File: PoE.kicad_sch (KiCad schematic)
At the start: 73 parts, among them Q2 FDMS86255, U20 TPS23734, U23 TCMT1107

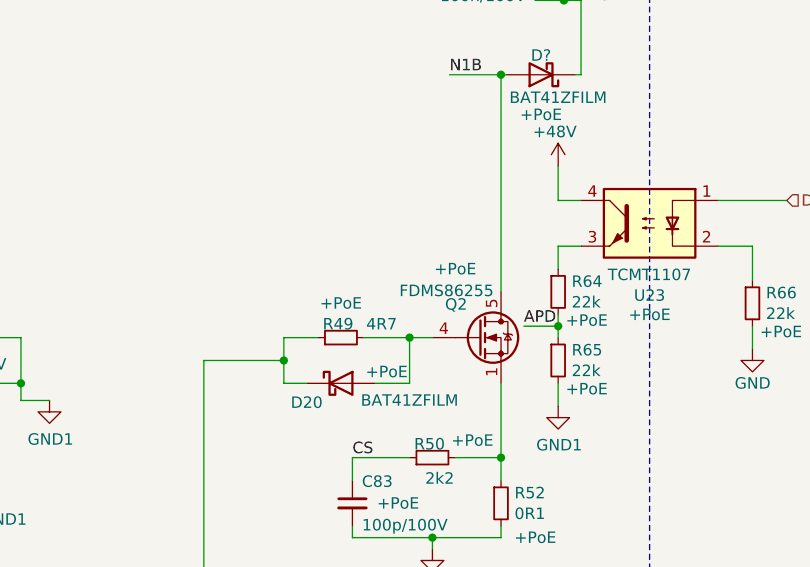
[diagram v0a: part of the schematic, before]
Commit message: Adjust Manufacturer/PartNumber for some parts
- Use Diodes B2100-13-F consistently
- Define part for pin headers
- Replace N-Channel MOSFET for PoE with BSZ440N10NS3GATMA1
- Define Input protection MOSFET DMP3013SFV-7

Signed-off-by: Stefan Agner <stefan@agner.ch>
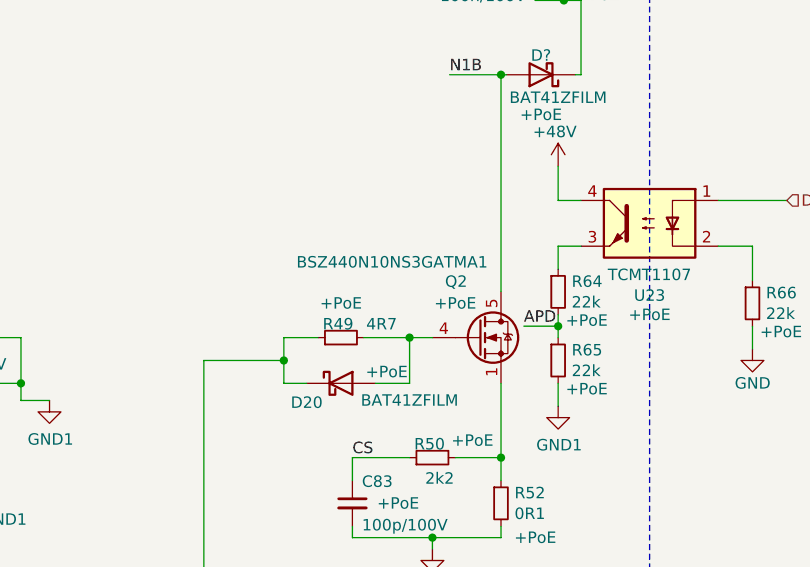
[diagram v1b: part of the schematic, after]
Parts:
- D18: PartNumber B3100-13-F -> B2100-13-F
- Q2: value FDMS86255 -> BSZ440N10NS3GATMA1; symbol Transistor_FET:FDMS86255 -> Transistor_FET:BSC440N10NS3G; Manufacturer ON Semiconductor -> Infineon Technologies; PartNumber FDMS86255 -> BSZ440N10NS3GATMA1
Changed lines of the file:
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@@
   (symbol (lib_id "power:GND1") (at 67.945 174.625 0) (unit 1)
     (in_bom yes) (on_board yes)
-    (property "Reference" "#PWR?" (id 0) (at 67.945 180.975 0)
+    (property "Reference" "#PWR0267" (id 0) (at 67.945 180.975 0)
       (effects (font (size 1.27 1.27)) hide)
     )
@@
   (symbol (lib_id "power:GND1") (at 121.92 129.54 90) (unit 1)
     (in_bom yes) (on_board yes)
-    (property "Reference" "#PWR?" (id 0) (at 128.27 129.54 0)
+    (property "Reference" "#PWR0270" (id 0) (at 128.27 129.54 0)
       (effects (font (size 1.27 1.27)) hide)
     )
@@
   (symbol (lib_id "power:GND1") (at 158.75 189.865 0) (unit 1)
     (in_bom yes) (on_board yes)
-    (property "Reference" "#PWR?" (id 0) (at 158.75 196.215 0)
+    (property "Reference" "#PWR0264" (id 0) (at 158.75 196.215 0)
       (effects (font (size 1.27 1.27)) hide)
     )
@@
   (symbol (lib_id "power:GND1") (at 165.1 64.77 0) (unit 1)
     (in_bom yes) (on_board yes)
-    (property "Reference" "#PWR?" (id 0) (at 165.1 71.12 0)
+    (property "Reference" "#PWR0269" (id 0) (at 165.1 71.12 0)
       (effects (font (size 1.27 1.27)) hide)
     )
@@
   (symbol (lib_id "power:GND1") (at 189.23 24.13 0) (unit 1)
     (in_bom yes) (on_board yes)
-    (property "Reference" "#PWR?" (id 0) (at 189.23 30.48 0)
+    (property "Reference" "#PWR0268" (id 0) (at 189.23 30.48 0)
       (effects (font (size 1.27 1.27)) hide)
     )
@@
   (symbol (lib_id "power:GND") (at 205.74 25.4 0) (unit 1)
     (in_bom yes) (on_board yes)
-    (property "Reference" "#PWR?" (id 0) (at 205.74 31.75 0)
+    (property "Reference" "#PWR0272" (id 0) (at 205.74 31.75 0)
       (effects (font (size 1.27 1.27)) hide)
     )
@@
   (symbol (lib_id "power:GND") (at 212.09 53.975 0) (unit 1)
     (in_bom yes) (on_board yes)
-    (property "Reference" "#PWR?" (id 0) (at 212.09 60.325 0)
+    (property "Reference" "#PWR0271" (id 0) (at 212.09 60.325 0)
       (effects (font (size 1.27 1.27)) hide)
     )
@@
   (symbol (lib_id "power:GND") (at 240.03 45.72 0) (unit 1)
     (in_bom yes) (on_board yes)
-    (property "Reference" "#PWR?" (id 0) (at 240.03 52.07 0)
+    (property "Reference" "#PWR0274" (id 0) (at 240.03 52.07 0)
       (effects (font (size 1.27 1.27)) hide)
     )
@@
   (symbol (lib_id "power:GND") (at 247.015 45.72 0) (unit 1)
     (in_bom yes) (on_board yes)
-    (property "Reference" "#PWR?" (id 0) (at 247.015 52.07 0)
+    (property "Reference" "#PWR0275" (id 0) (at 247.015 52.07 0)
       (effects (font (size 1.27 1.27)) hide)
     )
@@
   (symbol (lib_id "power:GND") (at 273.05 45.72 0) (unit 1)
     (in_bom yes) (on_board yes)
-    (property "Reference" "#PWR?" (id 0) (at 273.05 52.07 0)
+    (property "Reference" "#PWR0273" (id 0) (at 273.05 52.07 0)
       (effects (font (size 1.27 1.27)) hide)
     )
@@
       (effects (font (size 1.27 1.27)) hide)
     )
-    (property "PartNumber" "B3100-13-F" (id 6) (at 92.71 173.99 0)
+    (property "PartNumber" "B2100-13-F" (id 6) (at 92.71 173.99 0)
       (effects (font (size 1.27 1.27)) hide)
     )
@@
     (pin "2")
   )
-  (symbol (lib_id "Transistor_FET:FDMS86255") (at 180.34 109.22 0) (unit 1)
-    (in_bom yes) (on_board yes)
-    (property "Reference" "Q2" (id 0) (at 176.6571 105.5306 0)
-      (effects (font (size 1.27 1.27)) (justify left))
-    )
-    (property "Value" "FDMS86255" (id 1) (at 171.5771 104.0193 0)
+  (symbol (lib_id "Transistor_FET:BSC440N10NS3G") (at 180.34 109.22 0) (unit 1)
+    (in_bom yes) (on_board yes)
+    (property "Reference" "Q2" (id 0) (at 176.6571 102.9906 0)
+      (effects (font (size 1.27 1.27)) (justify left))
+    )
+    (property "Value" "BSZ440N10NS3GATMA1" (id 1) (at 160.1471 100.8443 0)
       (effects (font (size 1.27 1.27)) (justify left))
     )
@@
       (effects (font (size 1.27 1.27) italic) (justify left) hide)
     )
-    (property "Datasheet" "https://www.onsemi.com/pub/Collateral/FDMS86255-D.pdf" (id 3) (at 180.34 109.22 90)
+    (property "Datasheet" "http://www.infineon.com/dgdl/Infineon-BSC440N10NS3-DS-v02_04-en.pdf?fileId=db3a30432239cccd0122604520d47f56" (id 3) (at 180.34 109.22 90)
       (effects (font (size 1.27 1.27)) (justify left) hide)
     )
-    (property "Config" "+PoE" (id 4) (at 177.8 101.6 0))
-    (property "Manufacturer" "ON Semiconductor" (id 5) (at 180.34 109.22 0)
-      (effects (font (size 1.27 1.27)) hide)
-    )
-    (property "PartNumber" "FDMS86255" (id 6) (at 180.34 109.22 0)
-      (effects (font (size 1.27 1.27)) hide)
-    )
+    (property "Config" "+PoE" (id 4) (at 177.8 105.41 0))
+    (property "Manufacturer" "Infineon Technologies" (id 5) (at 180.34 109.22 0)
+      (effects (font (size 1.27 1.27)) hide)
+    )
+    (property "PartNumber" "BSZ440N10NS3GATMA1" (id 6) (at 180.34 109.22 0)
+      (effects (font (size 1.27 1.27)) hide)
+    )

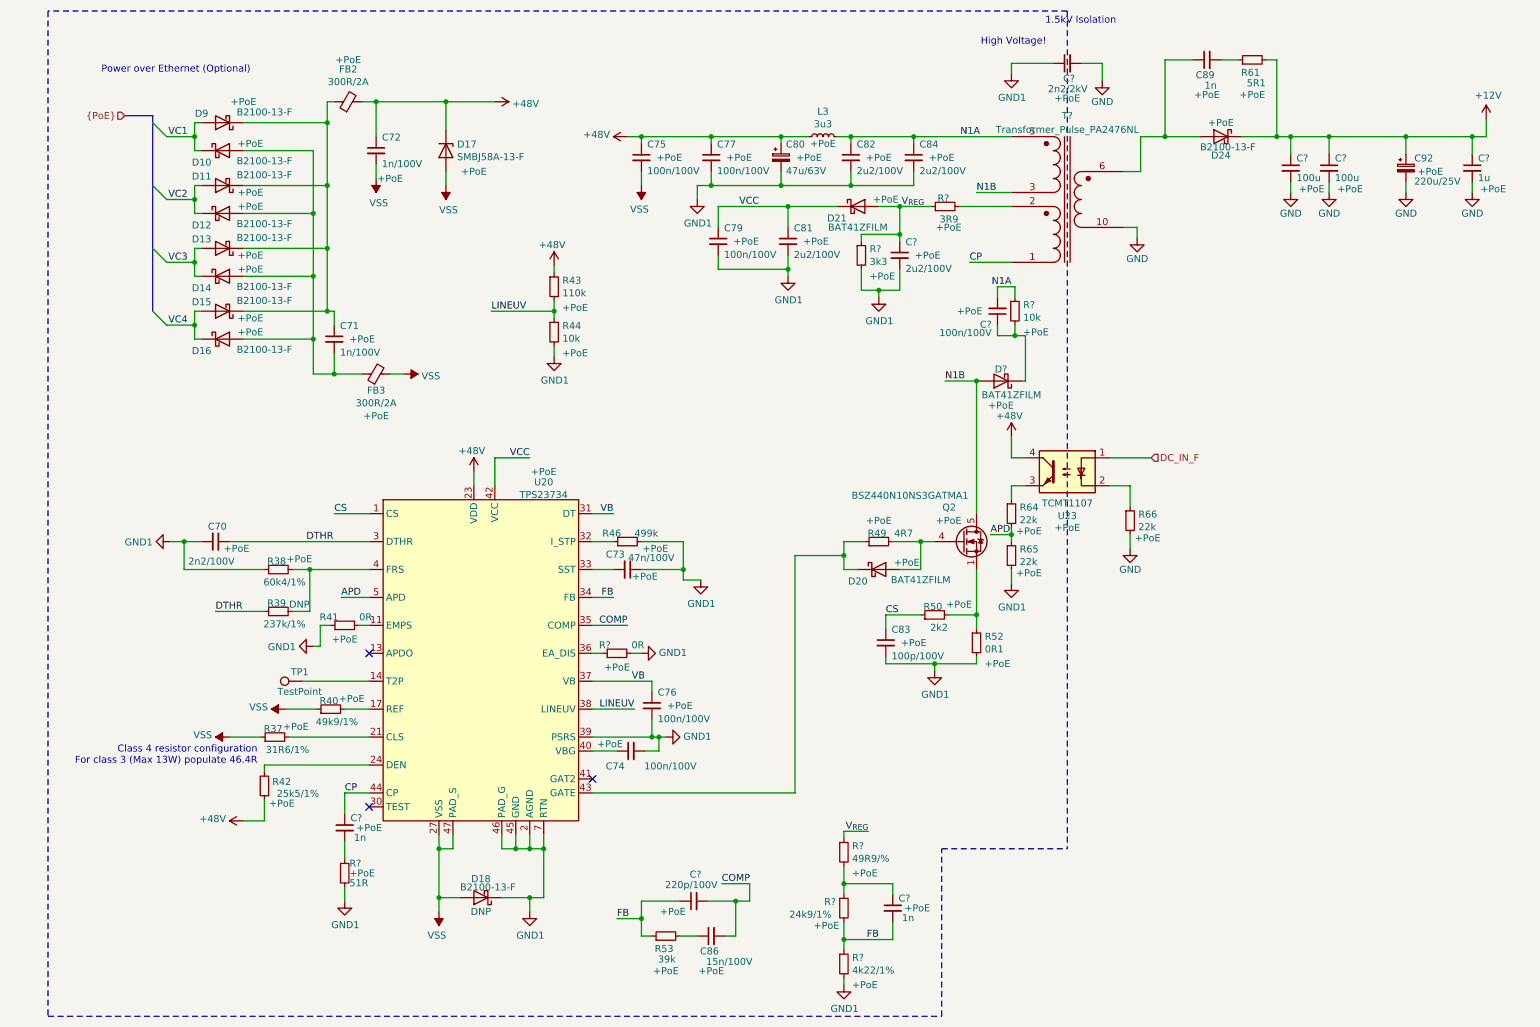
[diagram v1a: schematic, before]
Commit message: Adjust various parts to improve BOM
- Replace unusual/high value ceramics with lower value in parallel
- Use the same protection Shottky Diode in PoE as in regular input
  (B340LB-13-F)
- Replace PoE rectifier Diodes with B1100-13-F
- Replace PoE Inductor (SRN6045TA-3R3Y) with the same part from 5V power
  supply (Taiyo Yuden NRS8030T3R3MJGJ)
- Correctly specify Pulse Electronics transformer

Signed-off-by: Stefan Agner <stefan@agner.ch>
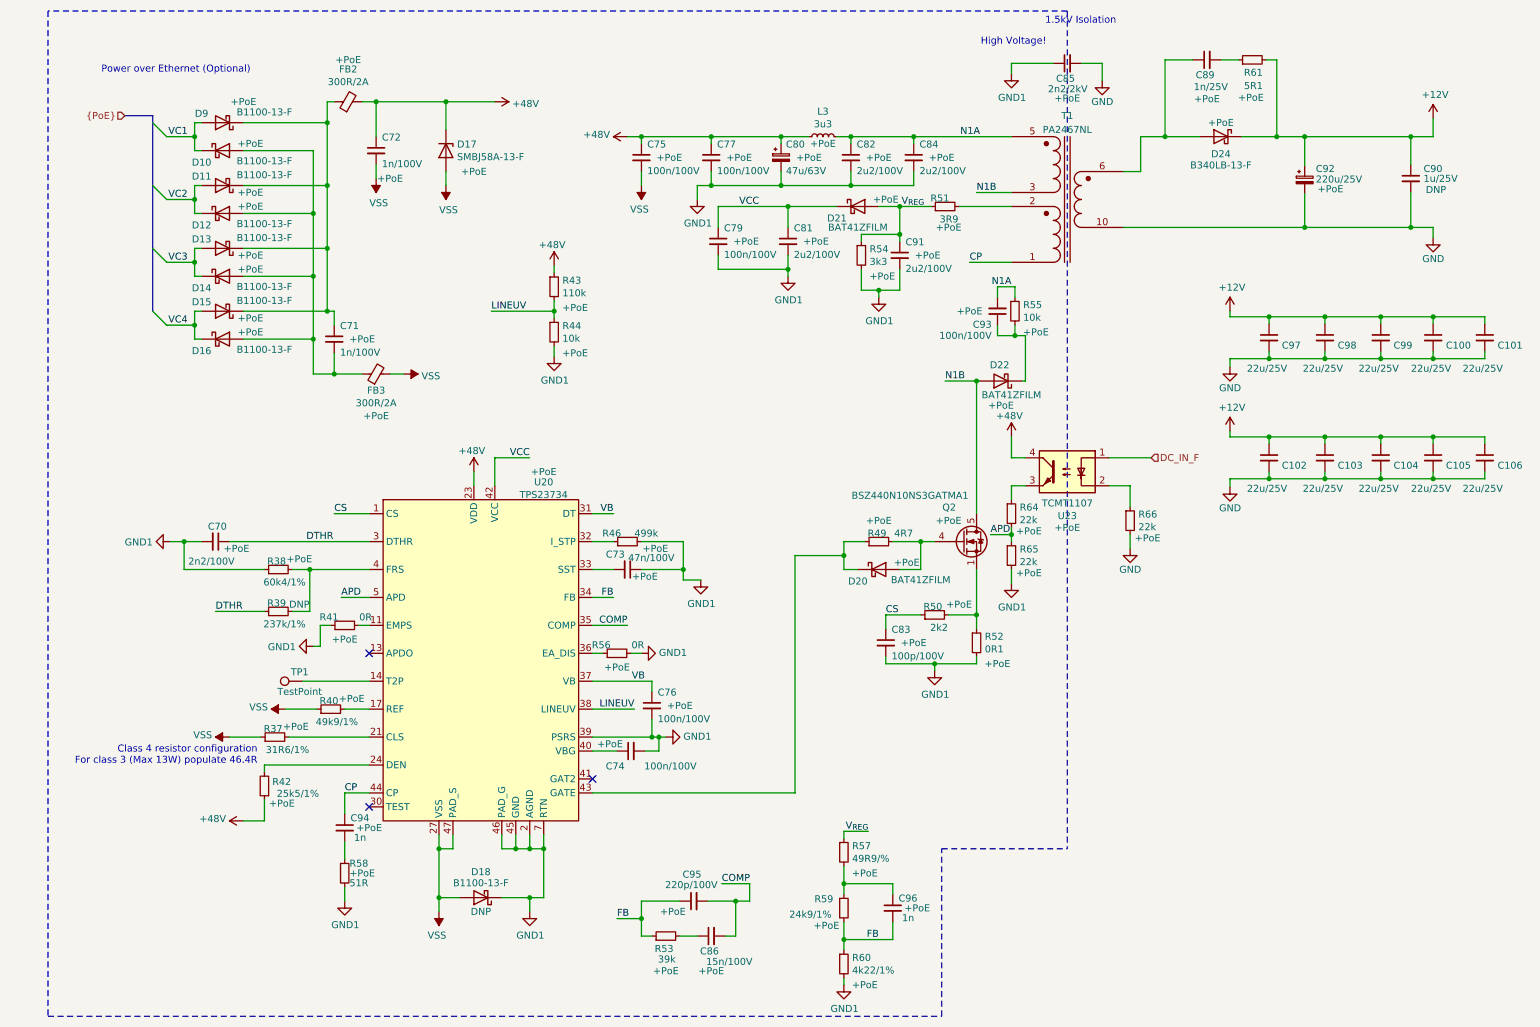
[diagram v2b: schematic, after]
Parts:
- removed C? (x2): 100u, Capacitor_SMD:C_0402_1005Metric, symbol Device:C_Small
- added C100, C101, C102, C103, C104, C105, C106, C97, C98, C99: 22u/25V, Capacitor_SMD:C_0805_2012Metric, symbol Device:C_Small
- C89: value 1n -> 1n/25V
- C90: renamed from C?; value 1u -> 1u/25V; Config +PoE -> DNP
- D10, D11, D12, D13, D14, D15, D16, D18, D9: value B2100-13-F -> B1100-13-F; footprint Diode_SMD:D_SMB -> Diode_SMD:D_SMA; PartNumber B2100-13-F -> B1100-13-F
- D24: value B2100-13-F -> B340LB-13-F; PartNumber B3100-13-F -> B340LB-13-F
- L3: footprint Inductor_SMD:L_Bourns_SRN6045TA -> Inductor_SMD:L_Taiyo-Yuden_NR-80xx; Manufacturer Bourns -> Taiyo Yuden; PartNumber SRN6045TA-3R3Y -> NRS8030T3R3MJGJ
- T1: renamed from T?; value Transformer_Pulse_PA2476NL -> PA2467NL; Manufacturer (none) -> Pulse Electronics; PartNumber (none) -> PA2467NL
- gave numbers to parts that had none: 15
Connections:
- net +12V: now also C100.1, C101.1, C102.1, C103.1, C104.1, C105.1, C106.1, C97.1, C98.1, C99.1
- net GND: now also C100.2, C101.2, C102.2, C103.2, C104.2, C105.2, C106.2, C97.2, C98.2, C99.2
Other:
- moved on the sheet: C90, C92

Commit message: Reannotate the complete schematics
Signed-off-by: Stefan Agner <stefan@agner.ch>
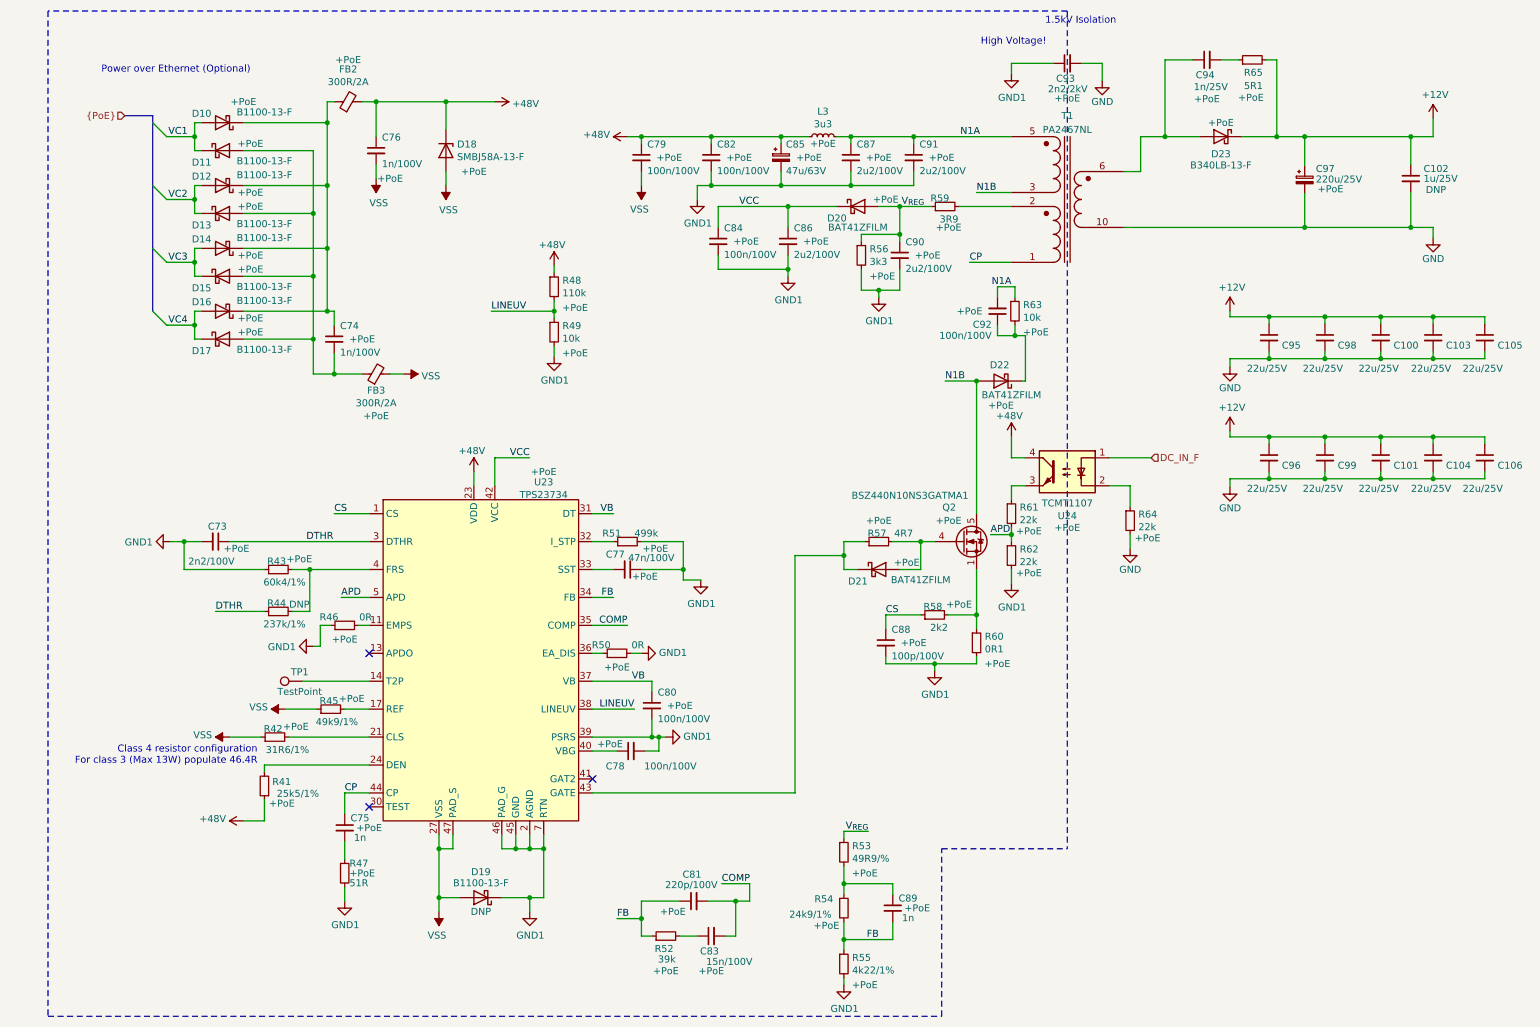
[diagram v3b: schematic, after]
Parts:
- renumbered C99 to C100, C104 to C101, C90 to C102, C100 to C103, C105 to C104, C101 to C105, C70 to C73, C71 to C74, C94 to C75, C72 to C76, C73 to C77, C74 to C78, C75 to C79, C76 to C80, C95 to C81, C77 to C82, C86 to C83, C79 to C84, C80 to C85, C81 to C86, C82 to C87, C83 to C88, C96 to C89, C91 to C90, C84 to C91, C93 to C92, C85 to C93, C89 to C94, C97 to C95, C102 to C96, C92 to C97, C103 to C99, D9 to D10, D10 to D11, D11 to D12, D12 to D13, D13 to D14, D14 to D15, D15 to D16, D16 to D17, D17 to D18, D18 to D19, D21 to D20, D20 to D21, D24 to D23, R42 to R41, R37 to R42, R38 to R43, R39 to R44, R40 to R45, R41 to R46, R58 to R47, R43 to R48, R44 to R49, R56 to R50, R46 to R51, R53 to R52, R57 to R53, R59 to R54, R60 to R55, R54 to R56, R49 to R57, R50 to R58, R51 to R59, R52 to R60, R64 to R61, R65 to R62, R55 to R63, R66 to R64, R61 to R65, U20 to U23, U23 to U24
